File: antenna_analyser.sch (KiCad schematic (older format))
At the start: 30 parts, among them IC1 MCP6002, IC2 ARDUINO_PRO_MINI_5V, P1 AD9850_CONN, P2 CONN_LCD, U1 AMS1117

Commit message: Added a switch for changing modes of operation, and a rotary encoder to change the frequency.
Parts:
- added S2: ENCODER, symbol ENCODER
- added SW1: SPST, symbol SPST
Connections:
- wire segments 124 -> 148
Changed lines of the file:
@@
 LIBS:AMS1117
 LIBS:ad9850_conn
+LIBS:switch-enc
 LIBS:antenna_analyser-cache
 EELAYER 25 0
@@
 $EndComp
 Wire Wire Line
-	7150 1350 7000 1350
-Wire Wire Line
-	7000 1350 7000 700
+	7000 1350 7150 1350
+Wire Wire Line
+	7000 700  7000 1350
 $Comp
 L GND #PWR08
@@
 Wire Wire Line
 	550  4500 700  4500
-Wire Wire Line
-	1300 4100 1100 4100
-Wire Wire Line
-	1300 4000 1050 4000
-Wire Wire Line
-	1300 3800 1000 3800
-Wire Wire Line
-	1300 3900 950  3900
 $Comp
 L R R2
@@
 Wire Wire Line
 	9550 2400 9550 2750
+Wire Wire Line
+	9550 4400 9550 6400
+Wire Wire Line
+	9550 6400 6800 6400
+Wire Wire Line
+	6800 6400 6800 7600
+Wire Wire Line
+	6800 7600 1050 7600
+Wire Wire Line
+	1050 7600 1050 3800
+Wire Wire Line
+	1050 3800 1300 3800
+Wire Wire Line
+	1300 3900 700  3900
+Wire Wire Line
+	700  3900 700  7500
+Wire Wire Line
+	700  7500 6700 7500
+Wire Wire Line
+	6700 7500 6700 6300
+Wire Wire Line
+	6700 6300 9450 6300
+Wire Wire Line
+	9450 6300 9450 4400
+Wire Wire Line
+	2400 4500 2650 4500
+Wire Wire Line
+	2650 4500 2650 7400
+Wire Wire Line
+	2650 7400 6600 7400
+Wire Wire Line
+	6600 7400 6600 6200
+Wire Wire Line
+	6600 6200 9350 6200
+Wire Wire Line
+	9350 6200 9350 4400
+Wire Wire Line
+	8950 4400 8950 5550
+$Comp
+L SPST SW1
+U 1 1 5597D09C
+P 7700 5400
+F 0 "SW1" H 7700 5500 50  0000 C CNN
+F 1 "SPST" H 7700 5300 50  0000 C CNN
+F 2 "" H 7700 5400 60  0000 C CNN
+F 3 "" H 7700 5400 60  0000 C CNN
+	1    7700 5400
+	1    0    0    -1
+$EndComp
+$Comp
+L GND #PWR?
+U 1 1 5597D150
+P 5950 6250
+F 0 "#PWR?" H 5950 6000 50  0001 C CNN
+F 1 "GND" H 5950 6100 50  0000 C CNN
+F 2 "" H 5950 6250 60  0000 C CNN
+F 3 "" H 5950 6250 60  0000 C CNN
+	1    5950 6250
+	1    0    0    -1
+$EndComp
+Wire Wire Line
+	8200 5400 9150 5400
+Wire Wire Line
+	9150 5400 9150 4400
+Wire Wire Line
+	7200 5400 5950 5400
+Wire Wire Line
+	5950 5400 5950 6250
+$Comp
+L ENCODER S2
+U 1 1 5597D6A6
+P 10550 5550
+F 0 "S2" H 10600 5900 50  0000 C CNN
+F 1 "ENCODER" H 10700 5200 50  0000 C CNN
+F 2 "" H 10550 5550 60  0000 C CNN
+F 3 "" H 10550 5550 60  0000 C CNN
+	1    10550 5550
+	1    0    0    -1
+$EndComp
+Wire Wire Line
+	9800 5550 5950 5550
+Connection ~ 5950 5550
+Wire Wire Line
+	10450 5000 9050 5000
+Wire Wire Line
+	9050 5000 9050 4400
+Wire Wire Line
+	10450 6100 9250 6100
+Wire Wire Line
+	9250 6100 9250 4400
+Connection ~ 8950 5550
 $EndSCHEMATC

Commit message: Removed KM library.
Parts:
- removed S2: ENCODER, symbol ENCODER
- removed SW1: SPST, symbol SPST
- added P3: CONN_01X05, symbol CONN_01X05
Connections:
- wire segments 148 -> 150
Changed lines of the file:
@@
 LIBS:AMS1117
 LIBS:ad9850_conn
-LIBS:switch-enc
 LIBS:antenna_analyser-cache
 EELAYER 25 0
@@
 Connection ~ 7000 850
 $Comp
-L GND #PWR?
+L GND #PWR012
 U 1 1 55904F2C
 P 9550 2050
-F 0 "#PWR?" H 9550 1800 50  0001 C CNN
+F 0 "#PWR012" H 9550 1800 50  0001 C CNN
 F 1 "GND" H 9550 1900 50  0000 C CNN
 F 2 "" H 9550 2050 60  0000 C CNN
@@
 	8950 4400 8950 5550
 $Comp
-L SPST SW1
-U 1 1 5597D09C
-P 7700 5400
-F 0 "SW1" H 7700 5500 50  0000 C CNN
-F 1 "SPST" H 7700 5300 50  0000 C CNN
-F 2 "" H 7700 5400 60  0000 C CNN
-F 3 "" H 7700 5400 60  0000 C CNN
-	1    7700 5400
-	1    0    0    -1
-$EndComp
-$Comp
-L GND #PWR?
+L GND #PWR013
 U 1 1 5597D150
 P 5950 6250
-F 0 "#PWR?" H 5950 6000 50  0001 C CNN
+F 0 "#PWR013" H 5950 6000 50  0001 C CNN
 F 1 "GND" H 5950 6100 50  0000 C CNN
 F 2 "" H 5950 6250 60  0000 C CNN
@@
 	1    0    0    -1
 $EndComp
-Wire Wire Line
-	8200 5400 9150 5400
-Wire Wire Line
-	9150 5400 9150 4400
-Wire Wire Line
-	7200 5400 5950 5400
-Wire Wire Line
-	5950 5400 5950 6250
-$Comp
-L ENCODER S2
-U 1 1 5597D6A6
-P 10550 5550
-F 0 "S2" H 10600 5900 50  0000 C CNN
-F 1 "ENCODER" H 10700 5200 50  0000 C CNN
-F 2 "" H 10550 5550 60  0000 C CNN
-F 3 "" H 10550 5550 60  0000 C CNN
-	1    10550 5550
-	1    0    0    -1
-$EndComp
-Wire Wire Line
-	9800 5550 5950 5550
-Connection ~ 5950 5550
-Wire Wire Line
-	10450 5000 9050 5000
-Wire Wire Line
-	9050 5000 9050 4400
-Wire Wire Line
-	10450 6100 9250 6100
-Wire Wire Line
-	9250 6100 9250 4400
 Connection ~ 8950 5550
+Wire Wire Line
+	5950 5550 10500 5550
+$Comp
+L CONN_01X05 P3
+U 1 1 5599C8E1
+P 10700 5550
+F 0 "P3" H 10700 5850 50  0000 C CNN
+F 1 "CONN_01X05" V 10800 5550 50  0000 C CNN
+F 2 "" H 10700 5550 60  0000 C CNN
+F 3 "" H 10700 5550 60  0000 C CNN
+	1    10700 5550
+	1    0    0    -1
+$EndComp
+Wire Wire Line
+	5950 5550 5950 6250
+Wire Wire Line
+	9050 4400 9050 5450
+Wire Wire Line
+	9050 5450 10500 5450
+Wire Wire Line
+	9150 4400 9150 5350
+Wire Wire Line
+	9150 5350 10500 5350
+Wire Wire Line
+	9250 4400 9250 5650
+Wire Wire Line
+	9250 5650 10500 5650
+Wire Wire Line
+	10500 5750 8200 5750
+Wire Wire Line
+	8200 5750 8200 1900
+Wire Wire Line
+	8200 1900 8950 1900
+Connection ~ 8950 1900
 $EndSCHEMATC

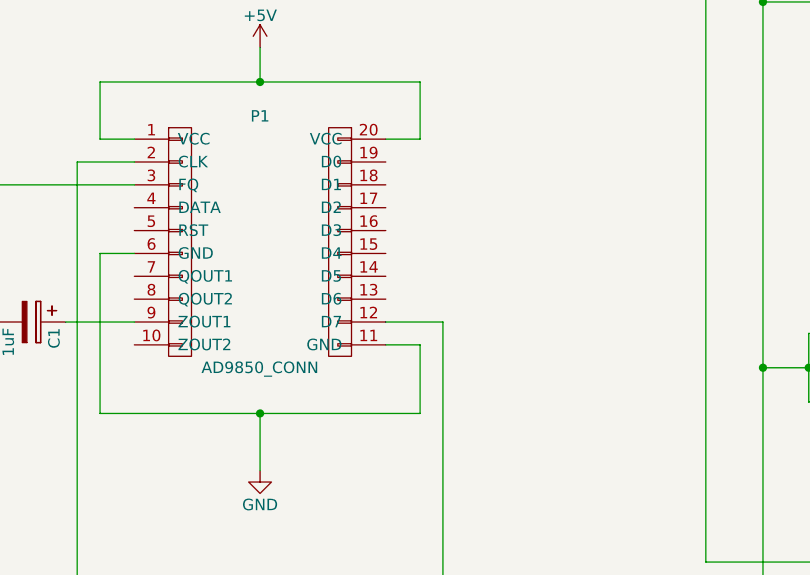
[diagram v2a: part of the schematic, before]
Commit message: Added an edge connector for the rotary encoder.
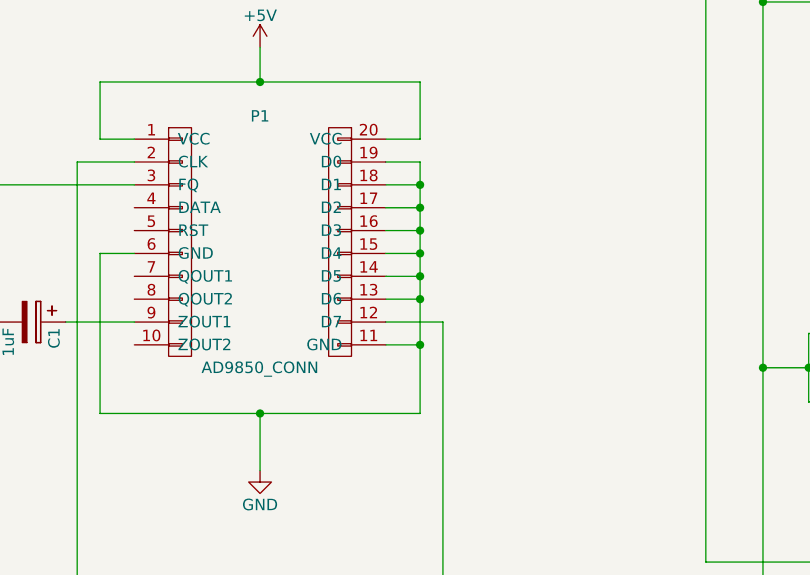
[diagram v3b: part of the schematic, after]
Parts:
- P1: footprint Pin_Headers:Pin_Header_Straight_1x10 -> dds-module-ad9850:DDS_AD9850
- P2: footprint (none) -> Pin_Headers:Pin_Header_Straight_1x15
- P3: footprint (none) -> Rotary-Encoders:BI_EN11-HSM1AF15
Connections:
- wire segments 150 -> 157
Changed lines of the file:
@@
 F 0 "P1" H 1850 4700 50  0000 C CNN
 F 1 "AD9850_CONN" H 1850 3600 50  0000 C CNN
-F 2 "Pin_Headers:Pin_Header_Straight_1x10" H 1500 4150 60  0001 C CNN
+F 2 "dds-module-ad9850:DDS_AD9850" H 1500 4150 60  0001 C CNN
 F 3 "" H 1500 4150 60  0000 C CNN
 	1    1500 4150
@@
 	1150 4900 2550 4900
 Wire Wire Line
-	2550 4900 2550 4600
+	2550 4900 2550 3800
 Wire Wire Line
 	2550 4600 2400 4600
@@
 F 0 "P2" H 10150 1800 50  0000 C CNN
 F 1 "CONN_LCD" V 10250 1000 50  0000 C CNN
-F 2 "" H 10150 1000 60  0000 C CNN
+F 2 "Pin_Headers:Pin_Header_Straight_1x15" H 10150 1000 60  0001 C CNN
 F 3 "" H 10150 1000 60  0000 C CNN
 	1    10150 1000
@@
 F 0 "P3" H 10700 5850 50  0000 C CNN
 F 1 "CONN_01X05" V 10800 5550 50  0000 C CNN
-F 2 "" H 10700 5550 60  0000 C CNN
+F 2 "Rotary-Encoders:BI_EN11-HSM1AF15" H 10700 5550 60  0001 C CNN
 F 3 "" H 10700 5550 60  0000 C CNN
 	1    10700 5550
@@
 	8200 1900 8950 1900
 Connection ~ 8950 1900
+Wire Wire Line
+	2550 3800 2400 3800
+Wire Wire Line
+	2550 4400 2400 4400
+Wire Wire Line
+	2400 4300 2550 4300
+Connection ~ 2550 4300
+Wire Wire Line
+	2400 4200 2550 4200
+Connection ~ 2550 4200
+Wire Wire Line
+	2400 4100 2550 4100
+Connection ~ 2550 4100
+Wire Wire Line
+	2400 4000 2550 4000
+Connection ~ 2550 4000
+Wire Wire Line
+	2400 3900 2550 3900
+Connection ~ 2550 3900
+Connection ~ 2550 4600
+Connection ~ 2550 4400
 $EndSCHEMATC

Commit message: PCB first attempt, no luck. Need to make sure the elements are on the correct side.
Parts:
- removed P3: CONN_01X05, Rotary-Encoders:BI_EN11-HSM1AF15, symbol CONN_01X05
- added ENC1: BI_EN11-HSM1AF15, Rotary-Encoders:BI_EN12-HS22AF30, symbol BI_EN11-HSM1AF15
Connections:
- wire segments 157 -> 159
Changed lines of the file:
@@
 LIBS:AMS1117
 LIBS:ad9850_conn
+LIBS:Rotary-Encoders
 LIBS:antenna_analyser-cache
 EELAYER 25 0
@@
 	9350 6200 9350 4400
 Wire Wire Line
-	8950 4400 8950 5550
+	8950 4400 8950 6000
 $Comp
 L GND #PWR013
@@
 Connection ~ 8950 5550
 Wire Wire Line
-	5950 5550 10500 5550
-$Comp
-L CONN_01X05 P3
-U 1 1 5599C8E1
-P 10700 5550
-F 0 "P3" H 10700 5850 50  0000 C CNN
-F 1 "CONN_01X05" V 10800 5550 50  0000 C CNN
-F 2 "Rotary-Encoders:BI_EN11-HSM1AF15" H 10700 5550 60  0001 C CNN
-F 3 "" H 10700 5550 60  0000 C CNN
-	1    10700 5550
-	1    0    0    -1
-$EndComp
-Wire Wire Line
 	5950 5550 5950 6250
-Wire Wire Line
-	9050 4400 9050 5450
-Wire Wire Line
-	9050 5450 10500 5450
-Wire Wire Line
-	9150 4400 9150 5350
-Wire Wire Line
-	9150 5350 10500 5350
-Wire Wire Line
-	9250 4400 9250 5650
-Wire Wire Line
-	9250 5650 10500 5650
-Wire Wire Line
-	10500 5750 8200 5750
-Wire Wire Line
-	8200 5750 8200 1900
-Wire Wire Line
-	8200 1900 8950 1900
-Connection ~ 8950 1900
 Wire Wire Line
 	2550 3800 2400 3800
@@
 Connection ~ 2550 4600
 Connection ~ 2550 4400
+$Comp
+L BI_EN11-HSM1AF15 ENC1
+U 1 1 559B7A1A
+P 10350 5550
+F 0 "ENC1" H 10350 5925 60  0000 C CNN
+F 1 "BI_EN11-HSM1AF15" H 10350 6050 60  0000 C CNN
+F 2 "Rotary-Encoders:BI_EN12-HS22AF30" H 10350 5550 60  0001 C CNN
+F 3 "" H 10350 5550 60  0000 C CNN
+	1    10350 5550
+	-1   0    0    1
+$EndComp
+Wire Wire Line
+	5950 5550 9800 5550
+Wire Wire Line
+	8950 6000 11000 6000
+Wire Wire Line
+	11000 6000 11000 5700
+Wire Wire Line
+	11000 5700 10900 5700
+Wire Wire Line
+	9050 4400 9050 5100
+Wire Wire Line
+	9050 5100 11000 5100
+Wire Wire Line
+	11000 5100 11000 5400
+Wire Wire Line
+	11000 5400 10900 5400
+Wire Wire Line
+	9800 5800 9150 5800
+Wire Wire Line
+	9150 5800 9150 4400
+Wire Wire Line
+	9800 5300 9250 5300
+Wire Wire Line
+	9250 5300 9250 4400
 $EndSCHEMATC

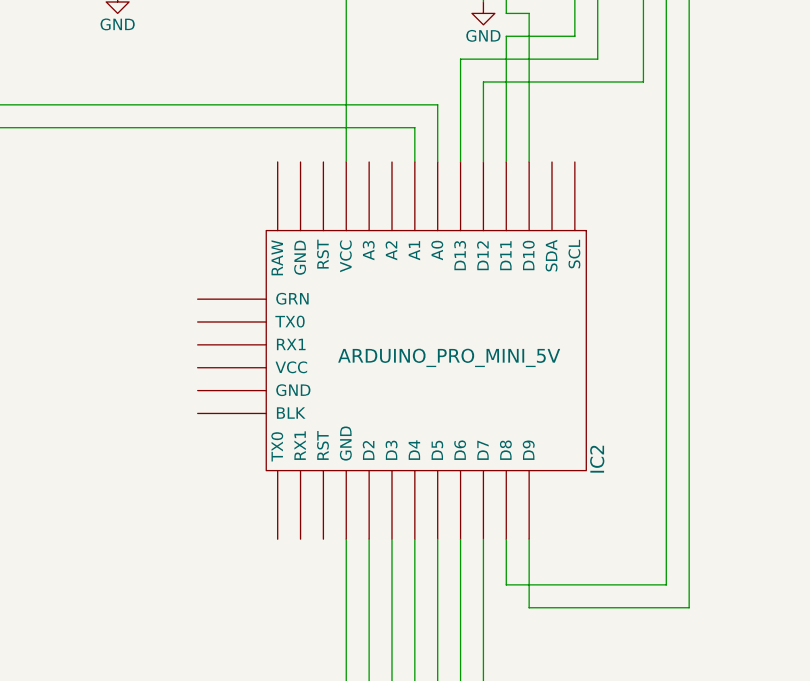
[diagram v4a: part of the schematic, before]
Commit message: MCP6002 is now properly attached on the PCB. The arduino board is attached as well. PCB needs work to be one-sided only.
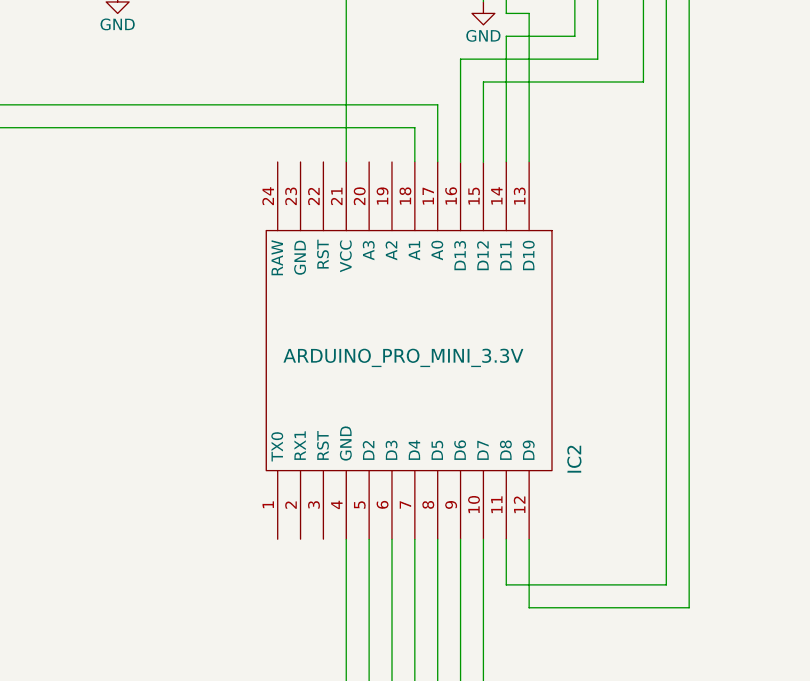
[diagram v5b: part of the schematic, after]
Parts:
- removed IC2: ARDUINO_PRO_MINI_5V, arduino pro mini:ARDUINO_PRO_MINI, symbol ARDUINO_PRO_MINI_5V
- added IC2: ARDUINO_PRO_MINI_3.3V, symbol ARDUINO_PRO_MINI_3.3V
- P2: footprint Pin_Headers:Pin_Header_Straight_1x15 -> Socket_Strips:Socket_Strip_Straight_1x15
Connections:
- net GND: now also IC2.4 (GND)
- net at IC1.1 (VoutA), R15.1, R16.1: now also IC2.18 (A1)
- net at IC1.7 (VoutB), R13.1, R14.1: now also IC2.17 (A0)
- net at P2.8 (P8), U1.2 (Vout): now also IC2.21 (VCC)
- net at P1.12 (D7): now also IC2.8 (D5)
- net at P1.2 (CLK): now also IC2.10 (D7)
- net at P1.3 (FQ): now also IC2.9 (D6)
- net at P2.3 (P3): now also IC2.13 (D10)
- net at P2.4 (P4): now also IC2.11 (D8)
- net at P2.5 (P5): now also IC2.12 (D9)
- net at P2.6 (P6): now also IC2.14 (D11)
- net at P2.7 (P7): now also IC2.16 (D13)
- net at P2.9 (P9): now also IC2.15 (D12)
- net at ENC1.A: now also IC2.6 (D3)
- net at ENC1.B: now also IC2.7 (D4)
- net at ENC1.SW2 (PB): now also IC2.5 (D2)
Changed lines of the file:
@@
 	0    -1   -1   0
-$EndComp
-$Comp
-L ARDUINO_PRO_MINI_5V IC2
-U 1 1 558DD335
-P 9250 3600
-F 0 "IC2" H 9700 4400 60  0000 C CNN
-F 1 "ARDUINO_PRO_MINI_5V" V 9250 3750 60  0000 C CNN
-F 2 "arduino pro mini:ARDUINO_PRO_MINI" H 9250 3600 60  0001 C CNN
-F 3 "" H 9250 3600 60  0000 C CNN
-	1    9250 3600
-	0    1    1    0
 $EndComp
 Wire Wire Line
@@
 F 0 "P2" H 10150 1800 50  0000 C CNN
 F 1 "CONN_LCD" V 10250 1000 50  0000 C CNN
-F 2 "Pin_Headers:Pin_Header_Straight_1x15" H 10150 1000 60  0001 C CNN
+F 2 "Socket_Strips:Socket_Strip_Straight_1x15" H 10150 1000 60  0001 C CNN
 F 3 "" H 10150 1000 60  0000 C CNN
 	1    10150 1000
@@
 Wire Wire Line
 	9250 5300 9250 4400
+$Comp
+L ARDUINO_PRO_MINI_3.3V IC2
+U 1 1 559C1201
+P 9250 3600
+F 0 "IC2" H 9700 4300 60  0000 C CNN
+F 1 "ARDUINO_PRO_MINI_3.3V" V 9250 3550 60  0000 C CNN
+F 2 "" H 9250 3600 60  0000 C CNN
+F 3 "" H 9250 3600 60  0000 C CNN
+	1    9250 3600
+	0    1    1    0
+$EndComp
 $EndSCHEMATC

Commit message: WIP
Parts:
- removed SMA_E1: SMA_EDGE, SMA_EDGE:SMA_EDGE, symbol SMA_EDGE
- added P4: BNC, symbol BNC
- added PWR1: CONN_01X02, symbol CONN_01X02
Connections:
- net +5V: now also PWR1.1 (P1)
- net GND: now also P4.2 (Ext), PWR1.2 (P2)
- net at C2.1, R10.1, R12.1: now also P4.1 (In)
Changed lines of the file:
@@
 Connection ~ 5250 1850
 Wire Wire Line
-	5100 1400 6350 1400
+	5100 1400 6300 1400
 Wire Wire Line
 	5250 1400 5250 1550
@@
 	0    1    1    0
 $EndComp
-$Comp
-L SMA_EDGE SMA_E1
-U 1 1 558B1D24
-P 6350 900
-F 0 "SMA_E1" H 6500 1200 60  0000 C CNN
-F 1 "SMA_EDGE" H 6500 1100 60  0000 C CNN
-F 2 "SMA_EDGE:SMA_EDGE" H 6350 900 60  0001 C CNN
-F 3 "" H 6350 900 60  0000 C CNN
-	1    6350 900
-	0    -1   -1   0
-$EndComp
 Wire Wire Line
 	9350 2750 9350 2500
@@
 L GND #PWR08
 U 1 1 558DDC04
-P 6350 2050
-F 0 "#PWR08" H 6350 1800 50  0001 C CNN
-F 1 "GND" H 6350 1900 50  0000 C CNN
-F 2 "" H 6350 2050 60  0000 C CNN
-F 3 "" H 6350 2050 60  0000 C CNN
-	1    6350 2050
+P 6450 2050
+F 0 "#PWR08" H 6450 1800 50  0001 C CNN
+F 1 "GND" H 6450 1900 50  0000 C CNN
+F 2 "" H 6450 2050 60  0000 C CNN
+F 3 "" H 6450 2050 60  0000 C CNN
+	1    6450 2050
 	1    0    0    -1
 $EndComp
@@
 Connection ~ 5450 2850
 Wire Wire Line
-	6250 1250 6250 1600
-Wire Wire Line
-	6250 1600 6450 1600
-Wire Wire Line
-	6450 1600 6450 1250
-Wire Wire Line
-	6350 1400 6350 1250
-Wire Wire Line
-	6350 2050 6350 1600
-Connection ~ 6350 1600
+	6450 1000 6450 2050
+Wire Wire Line
+	6300 1400 6300 800
 Wire Wire Line
 	4700 2600 4850 2600
@@
 	0    1    1    0
 $EndComp
+$Comp
+L CONN_01X02 PWR1
+U 1 1 559C0ACF
+P 2550 900
+F 0 "PWR1" H 2550 1050 50  0000 C CNN
+F 1 "CONN_01X02" V 2650 900 50  0000 C CNN
+F 2 "" H 2550 900 60  0000 C CNN
+F 3 "" H 2550 900 60  0000 C CNN
+	1    2550 900
+	1    0    0    -1
+$EndComp
+$Comp
+L +5V #PWR014
+U 1 1 559C0C97
+P 2200 750
+F 0 "#PWR014" H 2200 600 50  0001 C CNN
+F 1 "+5V" H 2200 890 50  0000 C CNN
+F 2 "" H 2200 750 60  0000 C CNN
+F 3 "" H 2200 750 60  0000 C CNN
+	1    2200 750
+	1    0    0    -1
+$EndComp
+$Comp
+L GND #PWR015
+U 1 1 559C0CCB
+P 2200 1050
+F 0 "#PWR015" H 2200 800 50  0001 C CNN
+F 1 "GND" H 2200 900 50  0000 C CNN
+F 2 "" H 2200 1050 60  0000 C CNN
+F 3 "" H 2200 1050 60  0000 C CNN
+	1    2200 1050
+	1    0    0    -1
+$EndComp
+Wire Wire Line
+	2350 950  2200 950
+Wire Wire Line
+	2200 950  2200 1050
+Wire Wire Line
+	2200 750  2200 850
+Wire Wire Line
+	2200 850  2350 850
+$Comp
+L BNC P4
+U 1 1 559C17A6
+P 6450 800
+F 0 "P4" H 6460 920 50  0000 C CNN
+F 1 "BNC" V 6560 740 50  0000 C CNN
+F 2 "" H 6450 800 60  0000 C CNN
+F 3 "" H 6450 800 60  0000 C CNN
+	1    6450 800
+	1    0    0    -1
+$EndComp
 $EndSCHEMATC

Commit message: Playing with freerouting, need to lay components according to a semi-planar schema and run freerouting on it.
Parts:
- IC2: footprint (none) -> arduino pro mini:ARDUINO_PRO_MINI
- P4, PWR1: footprint (none) -> Wire_Connections_Bridges:WireConnection_1mmDrill
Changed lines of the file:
@@
 F 0 "IC2" H 9700 4300 60  0000 C CNN
 F 1 "ARDUINO_PRO_MINI_3.3V" V 9250 3550 60  0000 C CNN
-F 2 "" H 9250 3600 60  0000 C CNN
+F 2 "arduino pro mini:ARDUINO_PRO_MINI" H 9250 3600 60  0001 C CNN
 F 3 "" H 9250 3600 60  0000 C CNN
 	1    9250 3600
@@
 F 0 "PWR1" H 2550 1050 50  0000 C CNN
 F 1 "CONN_01X02" V 2650 900 50  0000 C CNN
-F 2 "" H 2550 900 60  0000 C CNN
+F 2 "Wire_Connections_Bridges:WireConnection_1mmDrill" H 2550 900 60  0001 C CNN
 F 3 "" H 2550 900 60  0000 C CNN
 	1    2550 900
@@
 F 0 "P4" H 6460 920 50  0000 C CNN
 F 1 "BNC" V 6560 740 50  0000 C CNN
-F 2 "" H 6450 800 60  0000 C CNN
+F 2 "Wire_Connections_Bridges:WireConnection_1mmDrill" H 6450 800 60  0001 C CNN
 F 3 "" H 6450 800 60  0000 C CNN
 	1    6450 800

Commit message: 50/5k ohm resistors
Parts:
- removed P2: CONN_LCD, Socket_Strips:Socket_Strip_Straight_1x15, symbol CONN_01X15
- removed R1, R10, R2: 100, Resistors_ThroughHole:Resistor_Horizontal_RM10mm, symbol R
- removed R14, R16: 10k, Resistors_ThroughHole:Resistor_Horizontal_RM10mm, symbol R
- added P3: CONN_LCD, symbol CONN_01X09
- IC1: footprint sop8:SOP-8 -> Housings_DIP:DIP-8_W7.62mm
- P2: renamed from P4; footprint Wire_Connections_Bridges:WireConnection_1mmDrill -> Connect:bnc-ci
- R1: renamed from R3; value 100 -> 50
- R10: renamed from R13; value 10k -> 5k
- R11: renamed from R15; value 10k -> 5k
- R2: renamed from R6; value 100 -> 50
- R5: renamed from R12; value 100 -> 50
- renumbered C5 to C2, C2 to C5, R9 to R3, R5 to R4, R8 to R6, R4 to R7, R11 to R8, R7 to R9
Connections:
- net +5V: now also P3.1 (P1); no longer P1.20 (VCC)
- net GND: now also P3.2 (P2); no longer P1.11 (GND), P1.13 (D6), P1.14 (D5), P1.15 (D4), P1.16 (D3), P1.17 (D2), P1.18 (D1), P1.19 (D0)
- net at IC2.21 (VCC), U1.2 (Vout): now also P3.8 (P8)
- net at IC2.13 (D10): now also P3.3 (P3)
- net at IC2.14 (D11): now also P3.6 (P6)
- net at IC2.16 (D13): now also P3.7 (P7)
- net at IC2.15 (D12): now also P3.9 (P9)
- net at IC2.19 (A2): now also P3.4 (P4)
- net at IC2.20 (A3): now also P3.5 (P5)
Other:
- moved on the sheet: R1, R10, R11, R2, R5
